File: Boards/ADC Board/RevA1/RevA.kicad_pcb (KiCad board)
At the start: 2 copper layers, 85 x 56 mm, 31 parts, among them J1 Left Connector, J10 Jumper Terminals, J11 Arduino Nano, J12 Arduino Nano, J13 Extra Pins, J14 Screw Terminals, J16 Screw Terminals, J2 Right Connector, J3 Screw Terminals, J4 Jumper Terminals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

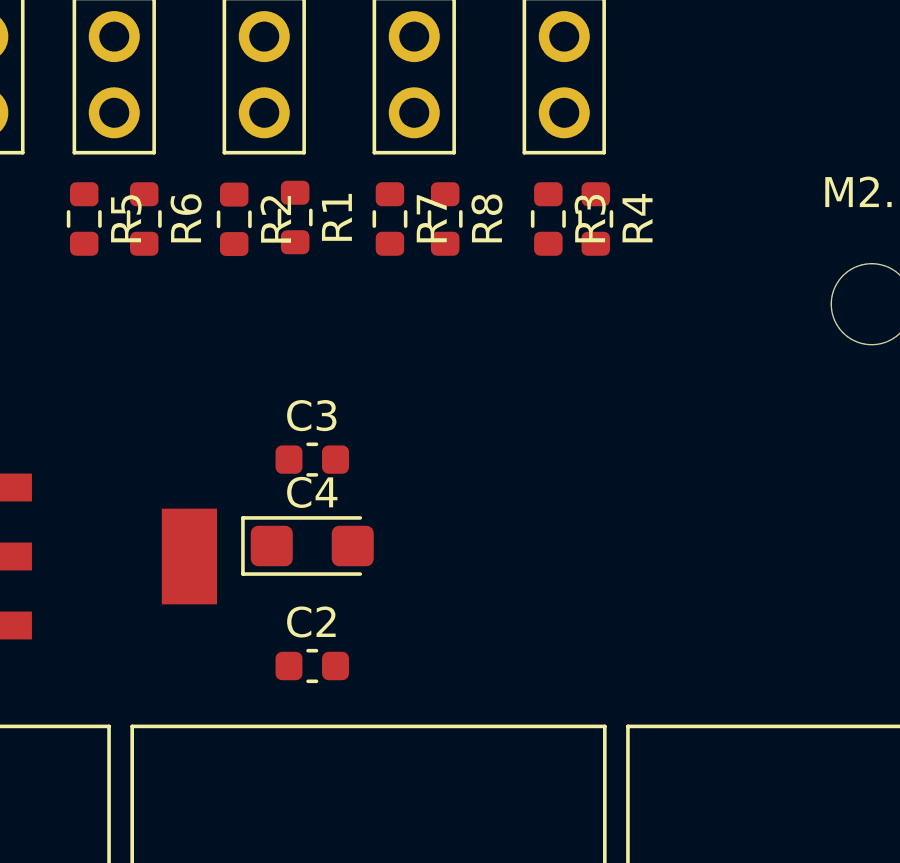
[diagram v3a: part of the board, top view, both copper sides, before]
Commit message: Moved around components on the ADC board PCB. Assigned footprints to microVolt board components.
Tried to add 6-pin spring connector to custom schematics list.
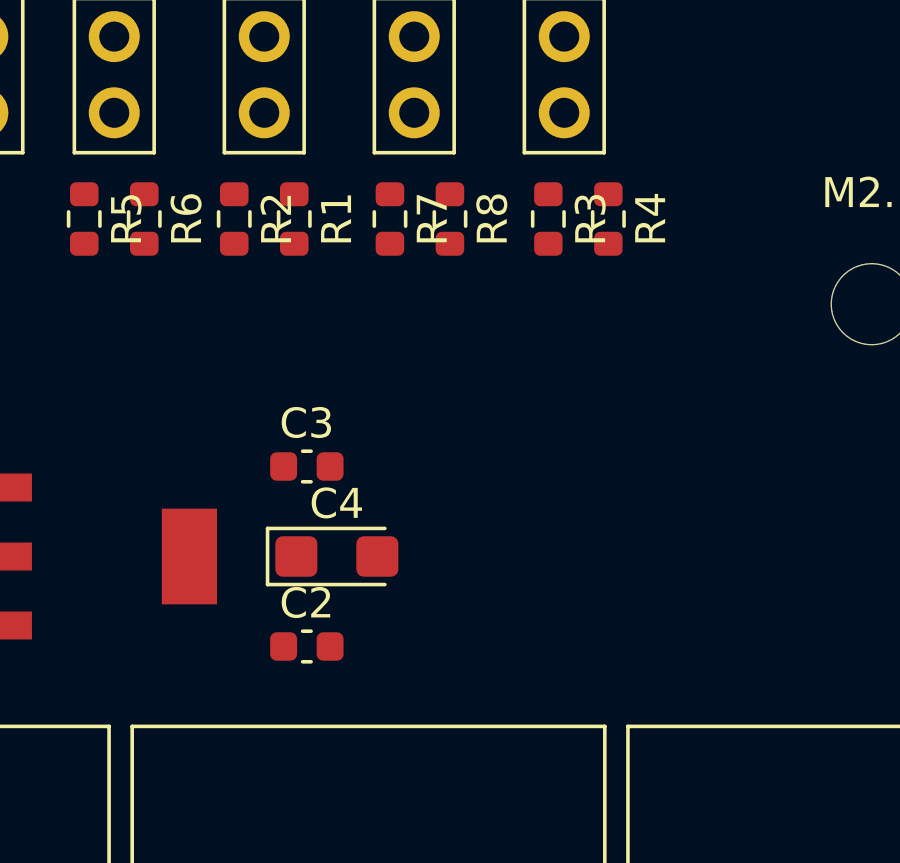
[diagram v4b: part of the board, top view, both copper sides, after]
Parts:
- moved C4 0.89 mm to (184.7, 106.4)
- moved C2 0.67 mm to (183.7, 109.4)
- moved R4 0.42 mm to (193.7, 95.2)
- moved C3 0.29 mm to (183.7, 103.4)
- moved R8 0.16 mm to (188.4, 95.2)
- moved R1 0.06 mm to (183.2, 95.2)
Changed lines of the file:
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@@
   )
   (module Capacitor_SMD:C_0603_1608Metric (layer F.Cu)
-    (at 183.85 110.06)
+    (at 183.67 109.41)
     (descr "Capacitor SMD 0603 (1608 Metric), square (rectangular) end terminal, IPC_7351 nominal, (Body size source: IPC-SM-782 page 76, https://www.pcb-3d.com/wordpress/wp-content/uploads/ipc-sm-782a_amendment_1_and_2.pdf), generated with kicad-footprint-generator")
     (tags capacitor)
@@
   )
   (module Capacitor_SMD:C_0603_1608Metric (layer F.Cu)
-    (at 183.85 103.18)
+    (at 183.67 103.41)
     (descr "Capacitor SMD 0603 (1608 Metric), square (rectangular) end terminal, IPC_7351 nominal, (Body size source: IPC-SM-782 page 76, https://www.pcb-3d.com/wordpress/wp-content/uploads/ipc-sm-782a_amendment_1_and_2.pdf), generated with kicad-footprint-generator")
     (tags capacitor)
@@
   )
   (module Capacitor_Tantalum_SMD:CP_EIA-3216-18_Kemet-A (layer F.Cu)
-    (at 183.85 106.06)
+    (at 184.67 106.41)
     (descr "Tantalum Capacitor SMD Kemet-A (3216-18 Metric), IPC_7351 nominal, (Body size from: http://www.kemet.com/Lists/ProductCatalog/Attachments/253/KEM_TC101_STD.pdf), generated with kicad-footprint-generator")
     (tags "capacitor tantalum")
@@
       (effects (font (size 1 1) (thickness 0.15)))
     )
-    (fp_line (start 1.6 -0.8) (end -1.2 -0.8) (layer F.Fab) (width 0.1))
-    (fp_line (start -1.2 -0.8) (end -1.6 -0.4) (layer F.Fab) (width 0.1))
-    (fp_line (start -1.6 -0.4) (end -1.6 0.8) (layer F.Fab) (width 0.1))
-    (fp_line (start -1.6 0.8) (end 1.6 0.8) (layer F.Fab) (width 0.1))
-    (fp_line (start 1.6 0.8) (end 1.6 -0.8) (layer F.Fab) (width 0.1))
-    (fp_line (start 1.6 -0.935) (end -2.31 -0.935) (layer F.SilkS) (width 0.12))
-    (fp_line (start -2.31 -0.935) (end -2.31 0.935) (layer F.SilkS) (width 0.12))
-    (fp_line (start -2.31 0.935) (end 1.6 0.935) (layer F.SilkS) (width 0.12))
-    (fp_line (start -2.3 1.05) (end -2.3 -1.05) (layer F.CrtYd) (width 0.05))
-    (fp_line (start -2.3 -1.05) (end 2.3 -1.05) (layer F.CrtYd) (width 0.05))
-    (fp_line (start 2.3 -1.05) (end 2.3 1.05) (layer F.CrtYd) (width 0.05))
-    (fp_line (start 2.3 1.05) (end -2.3 1.05) (layer F.CrtYd) (width 0.05))
     (fp_text user %R (at 0 0) (layer F.Fab)
       (effects (font (size 0.8 0.8) (thickness 0.12)))
     )
+    (fp_line (start 2.3 1.05) (end -2.3 1.05) (layer F.CrtYd) (width 0.05))
+    (fp_line (start 2.3 -1.05) (end 2.3 1.05) (layer F.CrtYd) (width 0.05))
+    (fp_line (start -2.3 -1.05) (end 2.3 -1.05) (layer F.CrtYd) (width 0.05))
+    (fp_line (start -2.3 1.05) (end -2.3 -1.05) (layer F.CrtYd) (width 0.05))
+    (fp_line (start -2.31 0.935) (end 1.6 0.935) (layer F.SilkS) (width 0.12))
+    (fp_line (start -2.31 -0.935) (end -2.31 0.935) (layer F.SilkS) (width 0.12))
+    (fp_line (start 1.6 -0.935) (end -2.31 -0.935) (layer F.SilkS) (width 0.12))
+    (fp_line (start 1.6 0.8) (end 1.6 -0.8) (layer F.Fab) (width 0.1))
+    (fp_line (start -1.6 0.8) (end 1.6 0.8) (layer F.Fab) (width 0.1))
+    (fp_line (start -1.6 -0.4) (end -1.6 0.8) (layer F.Fab) (width 0.1))
+    (fp_line (start -1.2 -0.8) (end -1.6 -0.4) (layer F.Fab) (width 0.1))
+    (fp_line (start 1.6 -0.8) (end -1.2 -0.8) (layer F.Fab) (width 0.1))
+    (pad 2 smd roundrect (at 1.35 0) (size 1.4 1.35) (layers F.Cu F.Paste F.Mask) (roundrect_rratio 0.185185)
+      (net 2 /GND))
     (pad 1 smd roundrect (at -1.35 0) (size 1.4 1.35) (layers F.Cu F.Paste F.Mask) (roundrect_rratio 0.185185)
       (net 3 /5V))
-    (pad 2 smd roundrect (at 1.35 0) (size 1.4 1.35) (layers F.Cu F.Paste F.Mask) (roundrect_rratio 0.185185)
-      (net 2 /GND))
     (model ${KISYS3DMOD}/Capacitor_Tantalum_SMD.3dshapes/CP_EIA-3216-18_Kemet-A.wrl
       (at (xyz 0 0 0))
@@
   )
   (module Resistor_SMD:R_0603_1608Metric (layer F.Cu)
-    (at 183.28 95.11 270)
+    (at 183.25 95.16 270)
     (descr "Resistor SMD 0603 (1608 Metric), square (rectangular) end terminal, IPC_7351 nominal, (Body size source: IPC-SM-782 page 72, https://www.pcb-3d.com/wordpress/wp-content/uploads/ipc-sm-782a_amendment_1_and_2.pdf), generated with kicad-footprint-generator")
     (tags resistor)
@@
   )
   (module Resistor_SMD:R_0603_1608Metric (layer F.Cu)
-    (at 181.25 95.17 270)
+    (at 181.25 95.16 270)
     (descr "Resistor SMD 0603 (1608 Metric), square (rectangular) end terminal, IPC_7351 nominal, (Body size source: IPC-SM-782 page 72, https://www.pcb-3d.com/wordpress/wp-content/uploads/ipc-sm-782a_amendment_1_and_2.pdf), generated with kicad-footprint-generator")
     (tags resistor)
@@
   )
   (module Resistor_SMD:R_0603_1608Metric (layer F.Cu)
-    (at 193.3 95.16 270)
+    (at 193.72 95.16 270)
     (descr "Resistor SMD 0603 (1608 Metric), square (rectangular) end terminal, IPC_7351 nominal, (Body size source: IPC-SM-782 page 72, https://www.pcb-3d.com/wordpress/wp-content/uploads/ipc-sm-782a_amendment_1_and_2.pdf), generated with kicad-footprint-generator")
     (tags resistor)
@@
   )
   (module Resistor_SMD:R_0603_1608Metric (layer F.Cu)
-    (at 188.28 95.16 270)
+    (at 188.44 95.16 270)
     (descr "Resistor SMD 0603 (1608 Metric), square (rectangular) end terminal, IPC_7351 nominal, (Body size source: IPC-SM-782 page 72, https://www.pcb-3d.com/wordpress/wp-content/uploads/ipc-sm-782a_amendment_1_and_2.pdf), generated with kicad-footprint-generator")
     (tags resistor)
@@
     (fp_text value "Screw Terminals" (at 5.25 0) (layer B.SilkS)
       (effects (font (size 1 1) (thickness 0.15)) (justify mirror))
-    )
-    (fp_text user * (at 0 0) (layer B.Fab)
-      (effects (font (size 1 1) (thickness 0.15)) (justify mirror))
-    )
-    (fp_text user * (at 0 0) (layer B.SilkS)
-      (effects (font (size 1 1) (thickness 0.15)) (justify mirror))
-    )
-    (fp_text user "Copyright 2021 Accelerated Designs. All rights reserved." (at 0 0) (layer Cmts.User)
-      (effects (font (size 0.127 0.127) (thickness 0.002)))
     )
     (fp_line (start -2.627 -4.826998) (end 13.127 -4.826998) (layer B.SilkS) (width 0.12))
@@
     (fp_circle (center -3.262 0) (end -2.881 0) (layer B.SilkS) (width 0.12))
     (fp_circle (center -3.262 0) (end -2.881 0) (layer F.SilkS) (width 0.12))
+    (fp_text user * (at 0 0) (layer B.Fab)
+      (effects (font (size 1 1) (thickness 0.15)) (justify mirror))
+    )
+    (fp_text user * (at 0 0) (layer B.SilkS)
+      (effects (font (size 1 1) (thickness 0.15)) (justify mirror))
+    )
+    (fp_text user "Copyright 2021 Accelerated Designs. All rights reserved." (at 0 0) (layer Cmts.User)
+      (effects (font (size 0.127 0.127) (thickness 0.002)))
+    )
     (pad 4 thru_hole circle (at 10.500002 0) (size 1.4986 1.4986) (drill 0.9906) (layers *.Cu *.Mask))
     (pad 3 thru_hole circle (at 7.000001 0) (size 1.4986 1.4986) (drill 0.9906) (layers *.Cu *.Mask)
@@
       (effects (font (size 1 1) (thickness 0.15)))
     )
-    (fp_text user * (at 0 0) (layer F.Fab)
-      (effects (font (size 1 1) (thickness 0.15)))
-    )
-    (fp_text user * (at 0 0) (layer F.SilkS)
-      (effects (font (size 1 1) (thickness 0.15)))
-    )
-    (fp_text user "Copyright 2021 Accelerated Designs. All rights reserved." (at 0 0) (layer Cmts.User)
-      (effects (font (size 0.127 0.127) (thickness 0.002)))
-    )
     (fp_line (start -2.627 4.826998) (end 13.127 4.826998) (layer F.SilkS) (width 0.12))
     (fp_line (start 13.127 4.826998) (end 13.127 -7.427001) (layer F.SilkS) (width 0.12))
@@
     (fp_circle (center -3.262 0) (end -2.881 0) (layer F.SilkS) (width 0.12))
     (fp_circle (center -3.262 0) (end -2.881 0) (layer B.SilkS) (width 0.12))
+    (fp_text user * (at 0 0) (layer F.Fab)
+      (effects (font (size 1 1) (thickness 0.15)))
+    )
+    (fp_text user * (at 0 0) (layer F.SilkS)
+      (effects (font (size 1 1) (thickness 0.15)))
+    )
+    (fp_text user "Copyright 2021 Accelerated Designs. All rights reserved." (at 0 0) (layer Cmts.User)
+      (effects (font (size 0.127 0.127) (thickness 0.002)))
+    )
     (pad 4 thru_hole circle (at 10.500002 0) (size 1.4986 1.4986) (drill 0.9906) (layers *.Cu *.Mask))
     (pad 3 thru_hole circle (at 7.000001 0) (size 1.4986 1.4986) (drill 0.9906) (layers *.Cu *.Mask)
@@
   (gr_line (start 163.5 126) (end 241.5 126) (layer Edge.Cuts) (width 0.1))
   (gr_line (start 160 122.5) (end 160 73.5) (layer Edge.Cuts) (width 0.1))
+  (zone (net 0) (net_name "") (layers F&B.Cu) (hatch edge 0.508)
+    (connect_pads (clearance 0.508))
+    (min_thickness 0.254)
+    (keepout (tracks not_allowed) (vias not_allowed) (copperpour allowed))
+    (fill (arc_segments 32) (thermal_gap 0.508) (thermal_bridge_width 0.508))
+    (polygon
+      (pts
+        (xy 202.9 95.32) (xy 203.38 95.44) (xy 203.77 95.61) (xy 204.17 95.87) (xy 204.48 96.16)
+        (xy 204.73 96.46) (xy 204.92 96.8) (xy 205.06 97.12) (xy 205.14 97.45) (xy 205.2 97.84)
+        (xy 205.19 98.31) (xy 205.11 98.73) (xy 204.94 99.17) (xy 204.73 99.53) (xy 204.46 99.86)
+        (xy 204.14 100.15) (xy 203.81 100.36) (xy 203.42 100.54) (xy 203 100.65) (xy 202.59 100.69)
+        (xy 202.14 100.68) (xy 201.7 100.58) (xy 201.26 100.4) (xy 200.84 100.13) (xy 200.49 99.81)
+        (xy 200.27 99.52) (xy 200.06 99.15) (xy 199.93 98.83) (xy 199.85 98.51) (xy 199.8 98.15)
+        (xy 199.82 97.66) (xy 199.9 97.28) (xy 200 97) (xy 200.04 96.88) (xy 200.13 96.73)
+        (xy 200.22 96.55) (xy 200.27 96.46) (xy 200.36 96.35) (xy 200.45 96.25) (xy 200.53 96.15)
+        (xy 200.65 96.03) (xy 200.73 95.97) (xy 200.84 95.87) (xy 200.94 95.8) (xy 201.06 95.73)
+        (xy 201.18 95.65) (xy 201.61 95.45) (xy 202.07 95.33) (xy 202.48 95.3)
+      )
+    )
+  )
 )

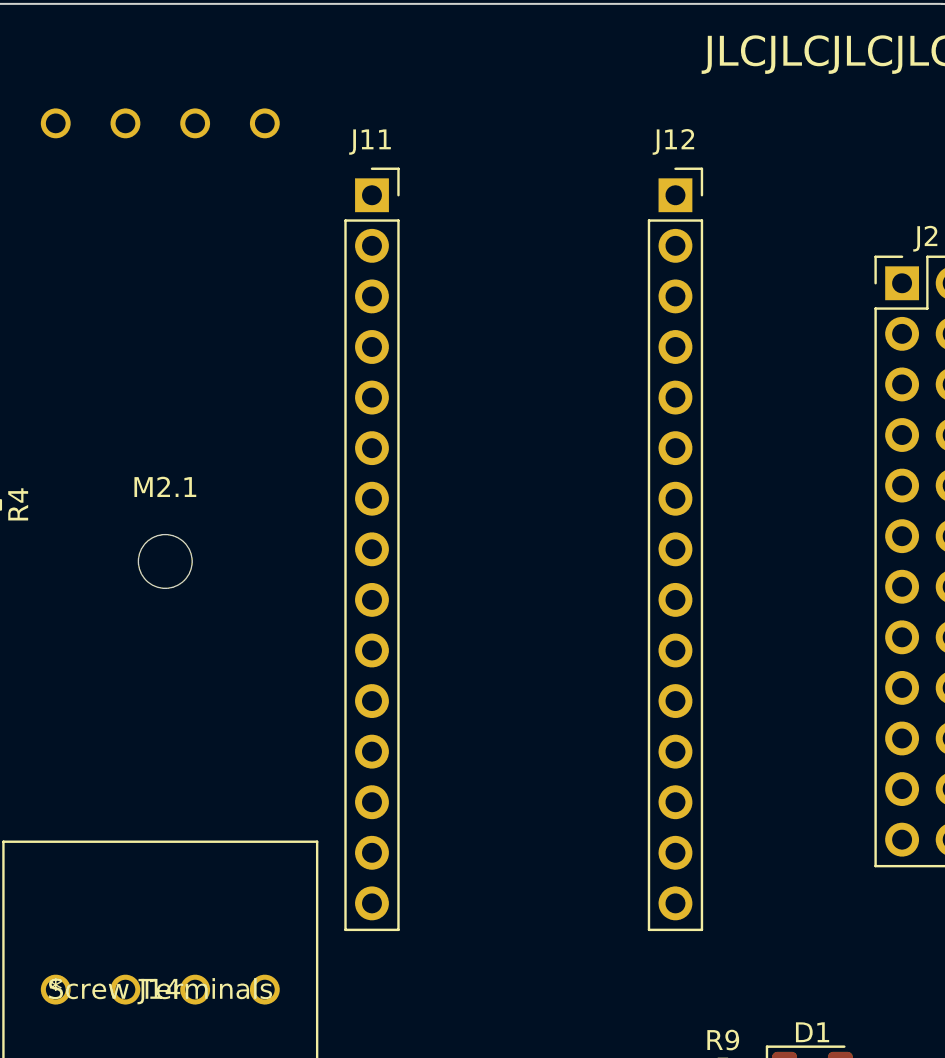
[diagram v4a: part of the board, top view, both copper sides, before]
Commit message: Created and layed out most of PCB for microvolt board. Removed one strain module, and added multiple mounting holes for the boards to be placed on.
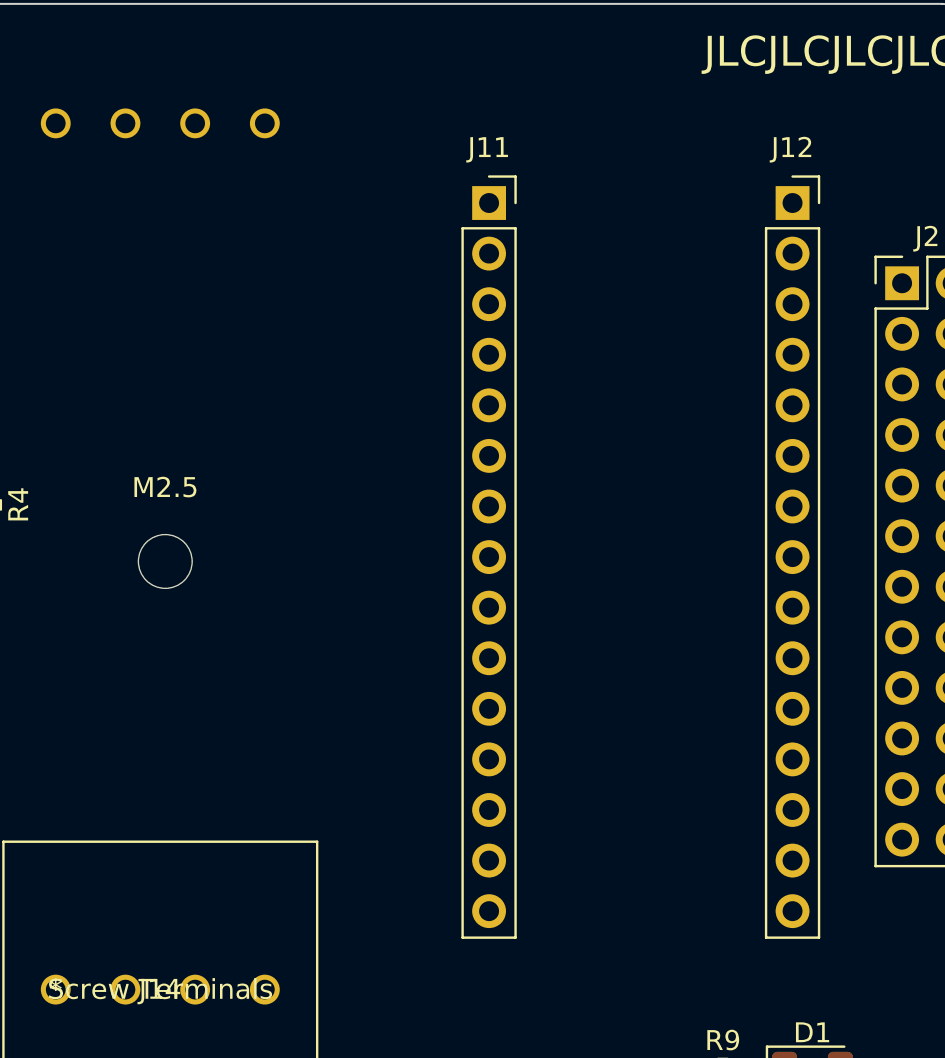
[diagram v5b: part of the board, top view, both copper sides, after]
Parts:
- moved J11 5.89 mm to (218.8, 80.0)
- moved J12 5.89 mm to (234.0, 80.0)
- renumbered M2.1 to M2.5
